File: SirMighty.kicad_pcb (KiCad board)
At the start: 2 copper layers, 61 x 20.5 mm, 49 parts, among them J1 Conn_01x20, J2 Conn_01x20, J3 USB_B_Micro, Q1 Q_DUAL_PMOS_S1G1D2S2G2D1, U2 AP7365-ADJ, U4 AP1117-50

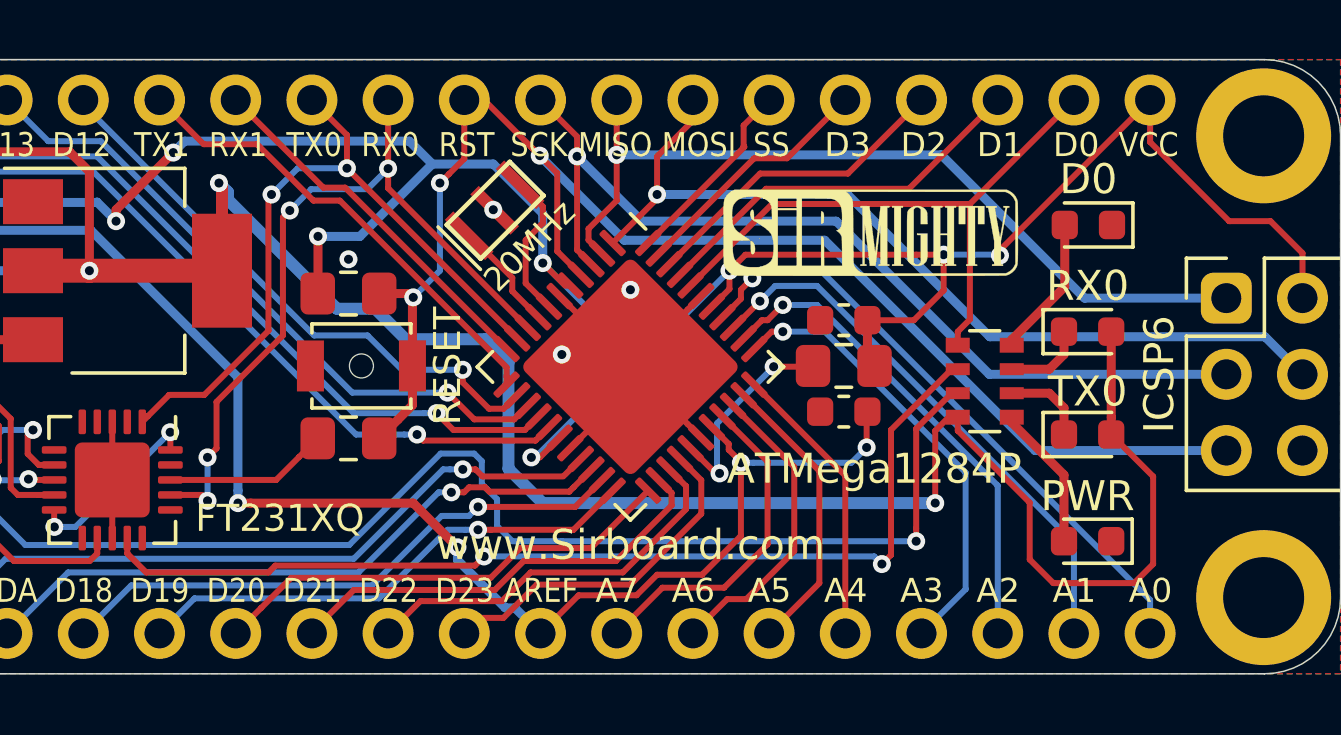
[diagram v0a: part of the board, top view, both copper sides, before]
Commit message: LDO capacitors edited
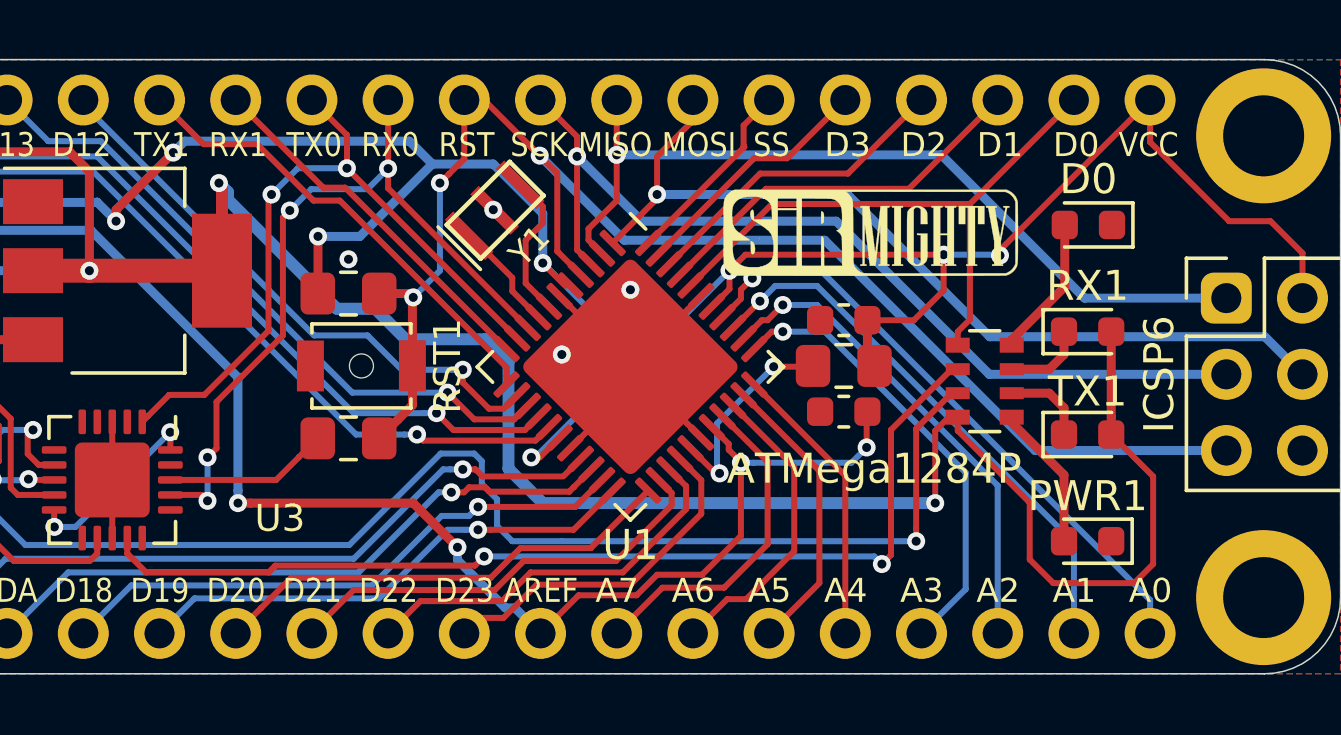
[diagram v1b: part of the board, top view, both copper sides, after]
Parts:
- C10: value 2.2uF -> 1uF
- U2: value AP7365-ADJ -> AP7365-W-7
- renumbered PWR to PWR1, RESET to RST1, RX0 to RX1, TX0 to TX1, www.Sirboard.com to U1, FT231XQ to U3, 20MHz to Y1
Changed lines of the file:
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@@
   (page A4)
   (layers
-    (0 F.Cu signal hide)
-    (31 B.Cu signal)
+    (0 F.Cu signal)
+    (31 B.Cu signal hide)
     (32 B.Adhes user hide)
     (33 F.Adhes user hide)
@@
     (tags "SMD SMT ceramic resonator filter")
     (attr smd)
-    (fp_text reference 20MHz (at -0.044901 1.661347 225) (layer F.SilkS)
+    (fp_text reference Y1 (at -0.044901 1.661347 225) (layer F.SilkS)
       (effects (font (size 0.8 0.8) (thickness 0.13)))
     )
@@
     (tags "QFN DFN_QFN")
     (attr smd)
-    (fp_text reference FT231XQ (at 1.28 -5.588) (layer F.SilkS)
+    (fp_text reference U3 (at 1.28 -5.588) (layer F.SilkS)
       (effects (font (size 0.9 0.9) (thickness 0.14)))
     )
@@
       (effects (font (size 0.8 0.8) (thickness 0.13)))
     )
-    (fp_text value AP7365-ADJ (at 0 2.9) (layer F.Fab)
+    (fp_text value AP7365-W-7 (at 0 2.9) (layer F.Fab)
       (effects (font (size 1 1) (thickness 0.15)))
     )
@@
     (tags "QFN DFN_QFN")
     (attr smd)
-    (fp_text reference www.Sirboard.com (at 4.199338 4.199338 180) (layer F.SilkS)
+    (fp_text reference U1 (at 4.199338 4.199338 180) (layer F.SilkS)
       (effects (font (size 1 1) (thickness 0.14)))
     )
@@
     (tags diode)
     (attr smd)
-    (fp_text reference TX0 (at 0 -1.43) (layer F.SilkS)
+    (fp_text reference TX1 (at 0 -1.43) (layer F.SilkS)
       (effects (font (size 1 1) (thickness 0.15)))
     )
@@
     (tags diode)
     (attr smd)
-    (fp_text reference RX0 (at 0 -1.524) (layer F.SilkS)
+    (fp_text reference RX1 (at 0 -1.524) (layer F.SilkS)
       (effects (font (size 1 1) (thickness 0.15)))
     )
@@
     (tags "Tactile Switch")
     (attr smd)
-    (fp_text reference RESET (at -2.8702 0 90) (layer F.SilkS)
+    (fp_text reference RST1 (at -2.8702 0 90) (layer F.SilkS)
       (effects (font (size 0.9 0.9) (thickness 0.14)))
     )
@@
     (tags diode)
     (attr smd)
-    (fp_text reference PWR (at 0.0006 1.4986) (layer F.SilkS)
+    (fp_text reference PWR1 (at 0.0006 1.4986) (layer F.SilkS)
       (effects (font (size 1 1) (thickness 0.15)))
     )
@@
       (effects (font (size 0.8 0.8) (thickness 0.13)))
     )
-    (fp_text value 2.2uF (at 0 1.65) (layer F.Fab)
-      (effects (font (size 1 1) (thickness 0.15)))
-    )
+    (fp_text value 1uF (at 0 1.65) (layer F.Fab)
+      (effects (font (size 1 1) (thickness 0.15)))
+    )

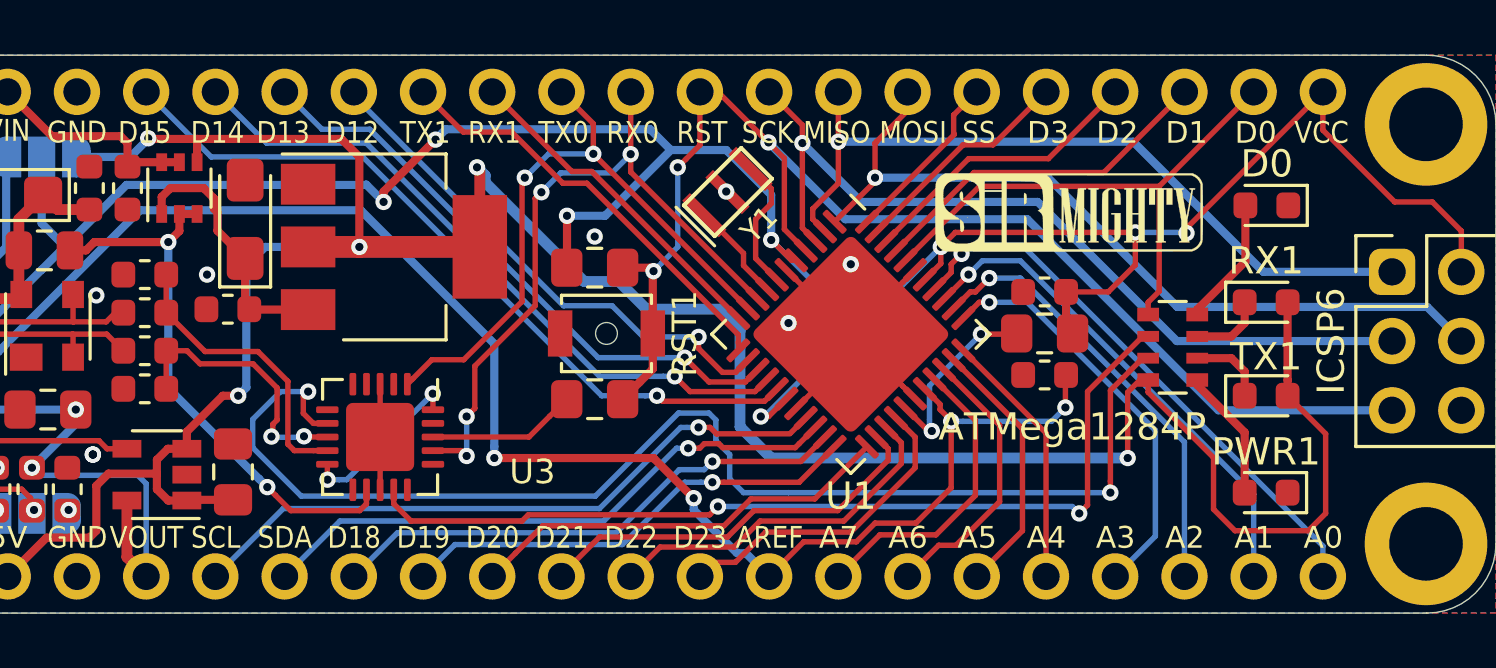
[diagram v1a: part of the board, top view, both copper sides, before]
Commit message: Capacitor Footprint changed
3216 to 3512
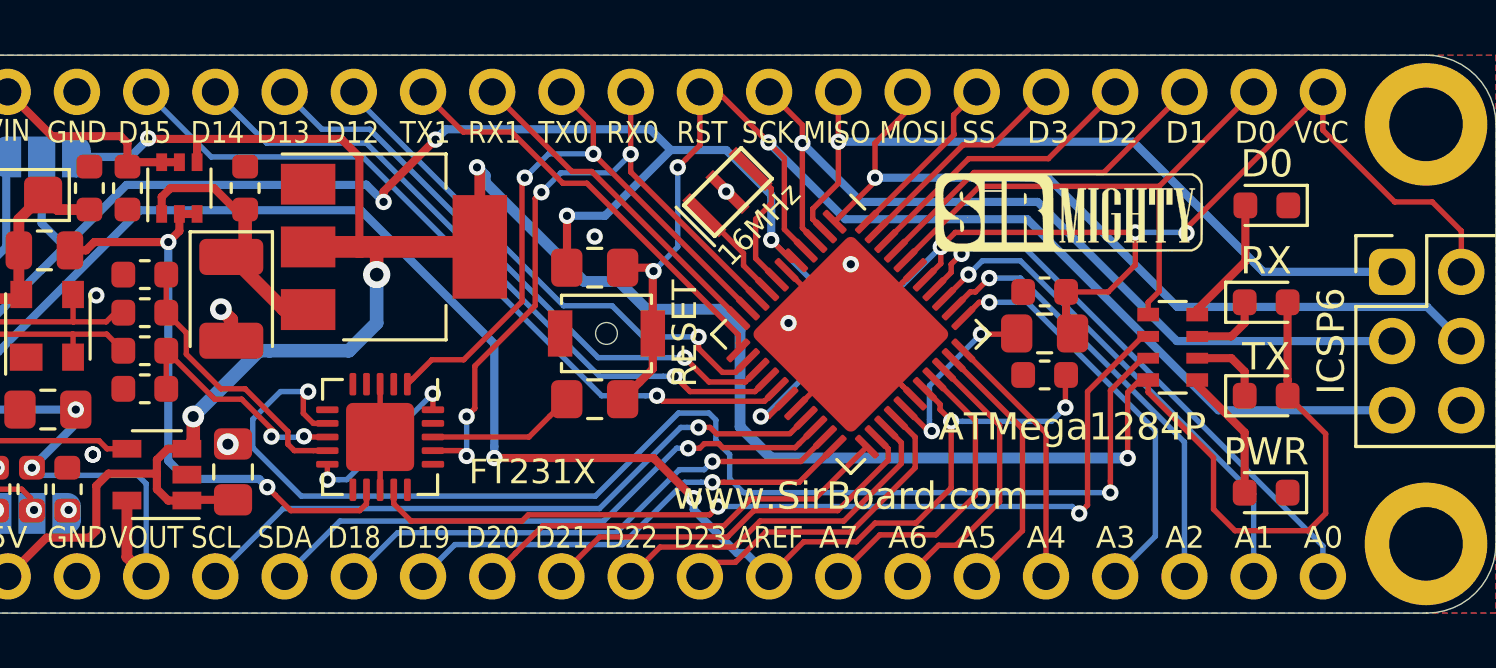
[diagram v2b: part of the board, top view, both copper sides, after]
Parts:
- C3: footprint Capacitor_Tantalum_SMD:CP_EIA-3216-18_Kemet-A_Pad1.58x1.35mm_HandSolder -> Capacitor_Tantalum_SMD:CP_EIA-3528-12_Kemet-T
- U4: value AP1117-50 -> AZ1117-5.0
- moved C5 4.49 mm to (144.9, 119.6), turned to 90 degrees
- moved C3 2.96 mm to (144.4, 123.7), turned to 270 degrees
- renumbered Y1 to 16MHz, U3 to FT231X, PWR1 to PWR, RST1 to RESET, RX1 to RX, TX1 to TX, U1 to www.SirBoard.com
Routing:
- net VUSB: track 20.7 -> 22.3 mm
- net GND: track 17.4 -> 18.7 mm, vias 9 -> 10
- net /uD+: track 9.93 -> 8.80 mm
- net /uD-: track 10.8 -> 10.1 mm
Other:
- rule pad_to_mask_clearance: 0.051 -> 0
- rule solder_mask_min_width: 0.25 -> 0.1

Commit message: Page Settings Updated
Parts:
- moved C10 122.1 mm to (48.6, 44.2)
- moved C11 122.1 mm to (68.7, 43.8)
- moved C5 122.1 mm to (55.9, 36.1)
- moved C6 122.1 mm to (50.2, 36.1)
- moved C8 122.1 mm to (47.1, 36.3)
- moved C9 122.1 mm to (55.4, 46.5)
- moved D1 122.1 mm to (48.6, 41.1)
- moved FT231X 122.1 mm to (60.8, 45.2)
- moved G*** 122.1 mm to (75.2, 41.4)
- moved G*** 122.1 mm to (51.3, 41.4)
- moved G*** 122.1 mm to (60.8, 41.4)
- moved G*** 122.1 mm to (86.1, 37.0)
- moved JP1 122.1 mm to (43.5, 41.4)
- moved JP3 122.1 mm to (48.4, 34.9)
- moved PWR 122.1 mm to (93.3, 47.2)
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
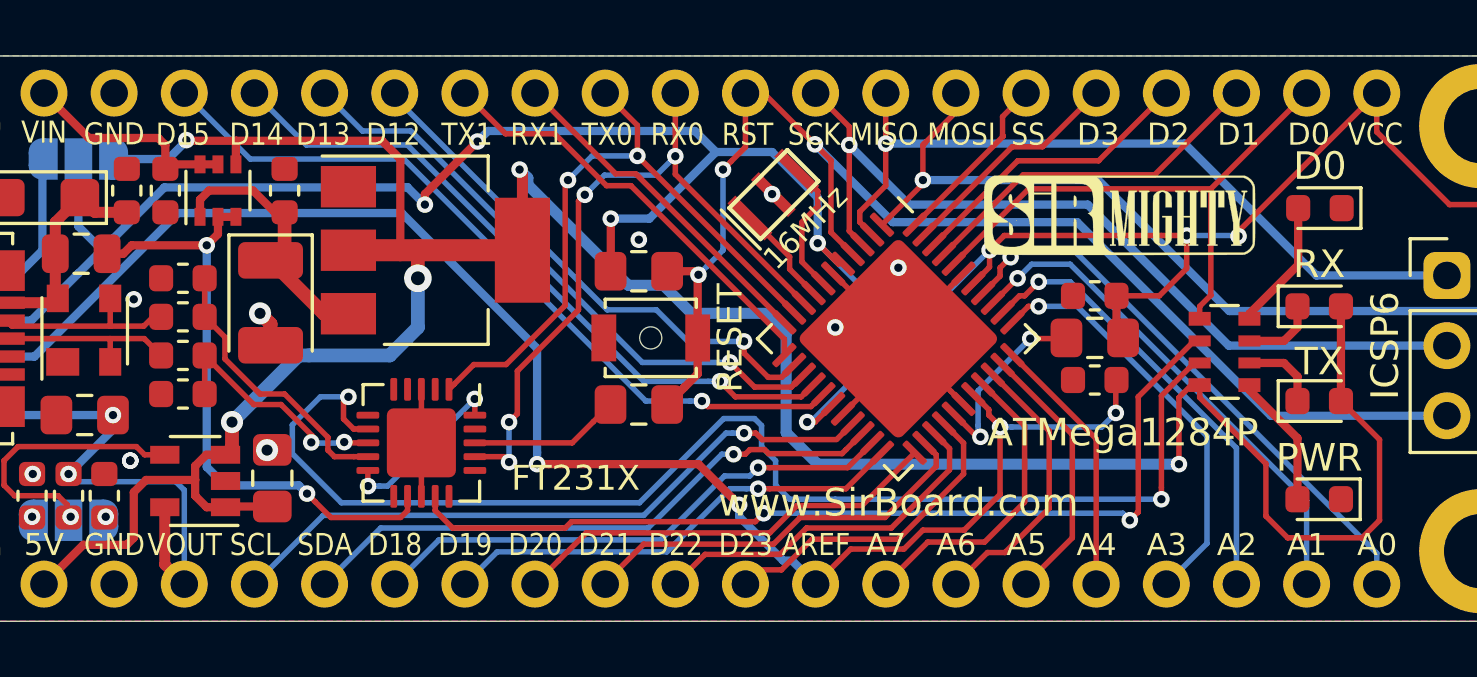
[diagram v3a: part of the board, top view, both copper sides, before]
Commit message: Part Numbers Added
Minor Board Revisions
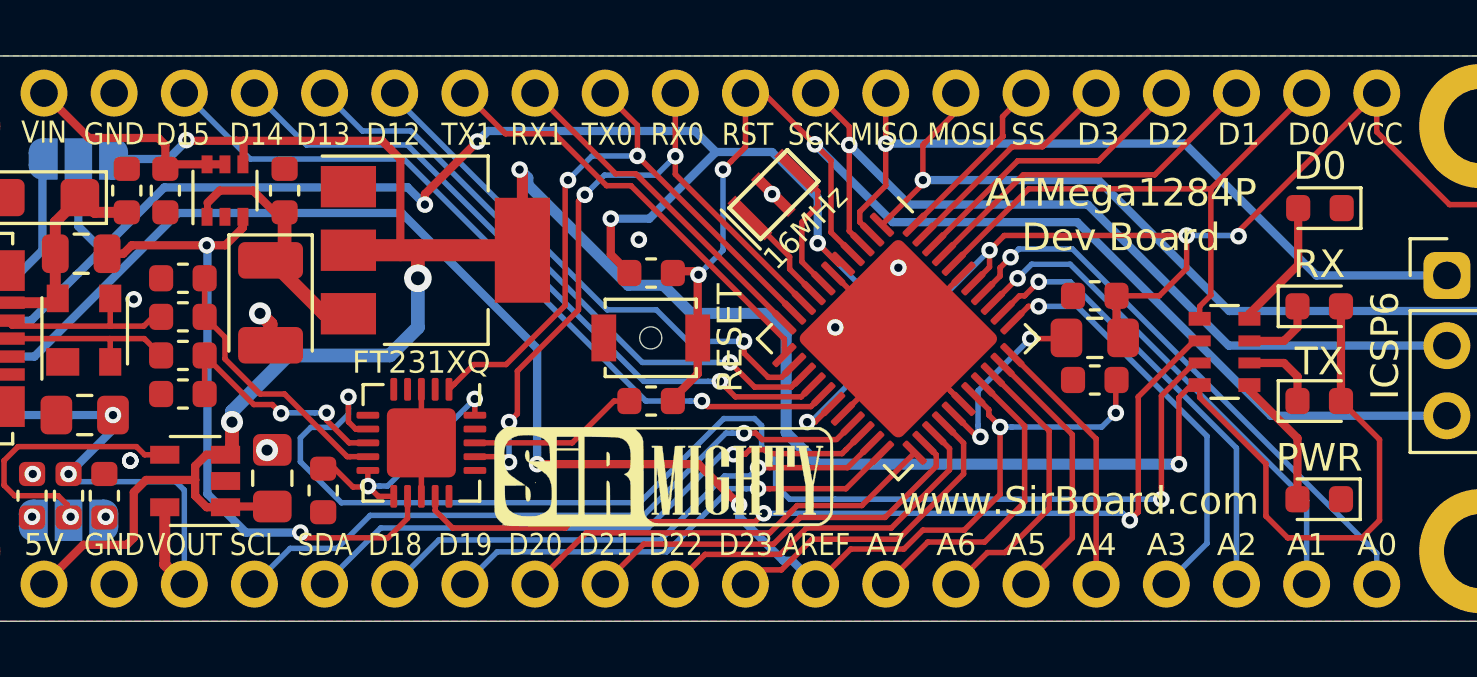
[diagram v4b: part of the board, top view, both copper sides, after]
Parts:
- removed the G*** at (86.1, 37.0)
- added C12: 100nF, Capacitor_SMD:C_0603_1608Metric, F.Cu at (57.3, 46.9)
- added G***: LOGO, logo:SirMighty132x36, F.Cu at (69.6, 46.4)
- 16MHz: value 20MHz -> 16MHz
- C11: footprint Capacitor_SMD:C_0805_2012Metric_Pad1.15x1.40mm_HandSolder -> Capacitor_SMD:C_0603_1608Metric
- R3: footprint Resistor_SMD:R_0805_2012Metric_Pad1.15x1.40mm_HandSolder -> Resistor_SMD:R_0603_1608Metric
- moved C11 0.46 mm to (69.2, 43.7)
- moved R3 0.45 mm to (69.2, 39.1)
- moved Q1 0.25 mm to (53.7, 36.1)
- renumbered FT231X to FT231XQ
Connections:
- FT231XQ pad 11: Net-(U3-Pad11) -> 3.3V
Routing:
- net 3.3V: track 6.33 -> 9.33 mm
- net VUSB: track 22.3 -> 23.7 mm
- net Net-(C11-Pad2): track 5.49 -> 6.22 mm
- net TX_LED: track 46.7 -> 46.2 mm
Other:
- board text added: "ATMega1284P Dev Board"
- board text removed: "ATMega1284P"
